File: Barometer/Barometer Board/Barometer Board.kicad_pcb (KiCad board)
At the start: 2 copper layers, 19 x 14.5 mm, 3 parts

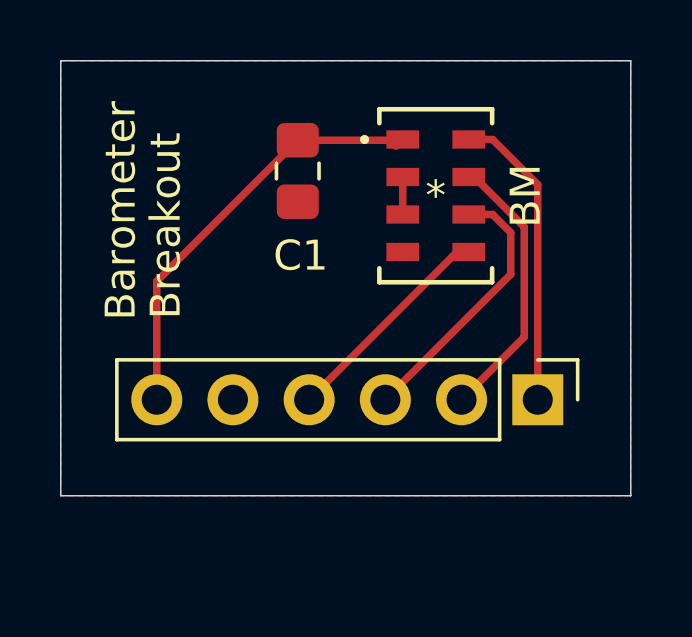
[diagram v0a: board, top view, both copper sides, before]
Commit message: Board Additions
Added the ground pour on bottom layer. Added no connect symbol on 4th pin. Added silk screen for pin outs
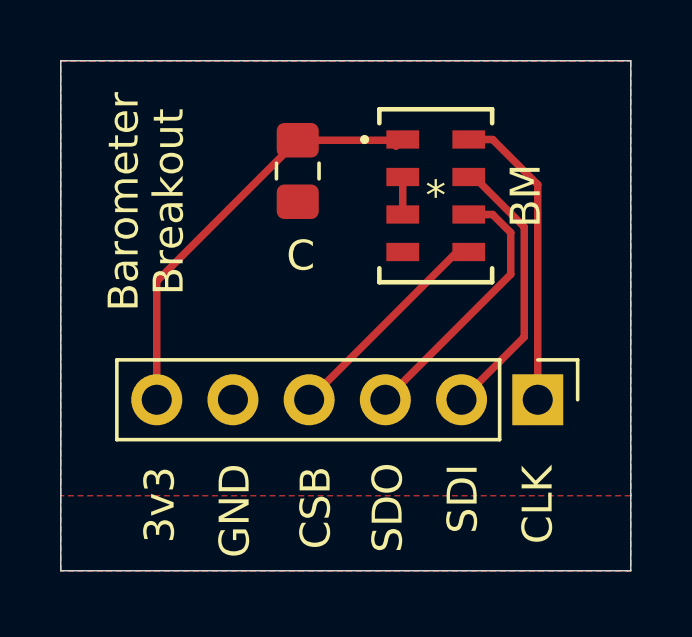
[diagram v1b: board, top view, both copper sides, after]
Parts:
- renumbered C1 to C
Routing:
- added copper zone on B.Cu, net GND
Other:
- board size 19 x 14.5 mm -> 19 x 17 mm
- board text added: "3v3"
- board text added: "CLK"
- board text added: "CSB"
- board text added: "GND"
- board text added: "SDI"
- board text added: "SDO"
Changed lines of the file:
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@@
   (general
     (thickness 1.6)
-    (drawings 6)
+    (drawings 15)
     (tracks 20)
     (zones 0)
@@
   (layers
     (0 F.Cu signal hide)
-    (31 B.Cu signal)
+    (31 B.Cu signal hide)
     (32 B.Adhes user)
     (33 F.Adhes user)
@@
     (pad_to_mask_clearance 0.05)
     (aux_axis_origin 0 0)
-    (visible_elements FFFFFF7F)
+    (visible_elements 7FFFFFFF)
     (pcbplotparams
       (layerselection 0x010fc_ffffffff)
@@
     (fp_text value MS560702BA03-50 (at 0 0) (layer F.Fab)
       (effects (font (size 1 1) (thickness 0.15)))
-    )
-    (fp_arc (start 0 -2.5019) (end 0.3048 -2.5019) (angle 180) (layer F.Fab) (width 0.1524))
-    (fp_text user * (at 0 0) (layer F.Fab)
-      (effects (font (size 1 1) (thickness 0.15)))
-    )
-    (fp_text user * (at 0 0) (layer F.SilkS)
-      (effects (font (size 1 1) (thickness 0.15)))
-    )
-    (fp_text user "Copyright 2016 Accelerated Designs. All rights reserved." (at 0 0) (layer Cmts.User)
-      (effects (font (size 0.127 0.127) (thickness 0.002)))
     )
     (fp_line (start -1.8796 2.8829) (end 1.8796 2.8829) (layer F.SilkS) (width 0.1524))
@@
     (fp_circle (center -2.3727 -1.875) (end -2.2965 -1.875) (layer F.SilkS) (width 0.1524))
     (fp_circle (center -0.254 -1.875) (end -0.1778 -1.875) (layer F.Fab) (width 0.1524))
+    (fp_arc (start 0 -2.5019) (end 0.3048 -2.5019) (angle 180) (layer F.Fab) (width 0.1524))
+    (fp_text user * (at 0 0) (layer F.Fab)
+      (effects (font (size 1 1) (thickness 0.15)))
+    )
+    (fp_text user * (at 0 0) (layer F.SilkS)
+      (effects (font (size 1 1) (thickness 0.15)))
+    )
+    (fp_text user "Copyright 2016 Accelerated Designs. All rights reserved." (at 0 0) (layer Cmts.User)
+      (effects (font (size 0.127 0.127) (thickness 0.002)))
+    )
     (pad 8 smd rect (at 1.1 -1.875) (size 1.0922 0.6096) (layers F.Cu F.Paste F.Mask)
       (net 7 /Barometer/CLK))
@@
     (tags "capacitor handsolder")
     (attr smd)
-    (fp_text reference C1 (at 2.825 -0.1 180) (layer F.SilkS)
+    (fp_text reference C (at 2.825 -0.1 180) (layer F.SilkS)
       (effects (font (size 1 1) (thickness 0.15)))
     )
@@
     )
   )
-  (gr_text Breakout (at 122 95 90) (layer F.SilkS)
-    (effects (font (size 1 1) (thickness 0.15)))
-  )
-  (gr_text Barometer (at 120.5 94.5 90) (layer F.SilkS)
+  (gr_line (start 137.5 106.5) (end 137.4 106.5) (layer Edge.Cuts) (width 0.05))
+  (gr_line (start 137.5 104) (end 137.5 106.5) (layer Edge.Cuts) (width 0.05))
+  (gr_line (start 118.5 106.5) (end 137.4 106.5) (layer Edge.Cuts) (width 0.05))
+  (gr_line (start 118.5 104) (end 118.5 106.5) (layer Edge.Cuts) (width 0.05))
+  (gr_text 3v3 (at 121.8 104.3 90) (layer F.SilkS)
+    (effects (font (size 1 1) (thickness 0.15)))
+  )
+  (gr_text GND (at 124.3 104.5 90) (layer F.SilkS)
+    (effects (font (size 1 1) (thickness 0.15)))
+  )
+  (gr_text CSB (at 127 104.4 90) (layer F.SilkS)
+    (effects (font (size 1 1) (thickness 0.15)))
+  )
+  (gr_text SDO (at 129.4 104.4 90) (layer F.SilkS)
+    (effects (font (size 1 1) (thickness 0.15)))
+  )
+  (gr_text CLK (at 134.4 104.3 90) (layer F.SilkS)
+    (effects (font (size 1 1) (thickness 0.15)))
+  )
+  (gr_text SDI (at 131.9 104.1 90) (layer F.SilkS)
+    (effects (font (size 1 1) (thickness 0.15)))
+  )
+  (gr_text Breakout (at 122.1 94.2 90) (layer F.SilkS)
+    (effects (font (size 1 1) (thickness 0.15)))
+  )
+  (gr_text Barometer (at 120.6 94.2 90) (layer F.SilkS)
     (effects (font (size 1 1) (thickness 0.15)))
   )
@@
   (gr_line (start 118.5 104) (end 118.5 89.5) (layer Edge.Cuts) (width 0.05))
   (gr_line (start 137.5 104) (end 137.5 89.5) (layer Edge.Cuts) (width 0.05))
-  (gr_line (start 118.5 104) (end 137.5 104) (layer Edge.Cuts) (width 0.05))
   (segment (start 129.675 92.35) (end 129.9 92.125) (width 0.25) (layer F.Cu) (net 1))
   (segment (start 129.875 92.15) (end 129.9 92.125) (width 0.25) (layer F.Cu) (net 1))
@@
       )
     )
+  )
+  (zone (net 2) (net_name GND) (layer F.Cu) (hatch edge 0.508)
+    (connect_pads (clearance 0.508))
+    (min_thickness 0.254)
+    (fill yes (arc_segments 32) (thermal_gap 0.508) (thermal_bridge_width 0.508))
+    (polygon
+      (pts
+        (xy 137.5 106.5) (xy 118.5 106.5) (xy 118.5 89.5) (xy 137.5 89.5)
+      )
+    )
+  )
+  (zone (net 2) (net_name GND) (layer F.Cu) (hatch edge 0.508)
+    (connect_pads (clearance 0.508))
+    (min_thickness 0.254)
+    (fill yes (arc_segments 32) (thermal_gap 0.508) (thermal_bridge_width 0.508))
+    (polygon
+      (pts
+        (xy 137.5 106.5) (xy 118.5 106.5) (xy 118.5 89.5) (xy 137.5 89.5)
+      )
+    )
+  )
+  (zone (net 2) (net_name GND) (layer B.Cu) (hatch edge 0.508)
+    (connect_pads (clearance 0.508))
+    (min_thickness 0.254)
+    (fill yes (arc_segments 32) (thermal_gap 0.508) (thermal_bridge_width 0.508))
+    (polygon
+      (pts
+        (xy 137.5 106.5) (xy 118.5 106.5) (xy 118.5 89.5) (xy 137.5 89.5)
+      )
+    )

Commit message: Fixed Minor Issues
BOOM!
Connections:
- net /Barometer/CLK renamed /Barometer/SCLK
- BM pad 4: Net-(Barometer201-Pad4) -> /Barometer/CSB
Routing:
- net /Barometer/CSB: track 7.36 -> 8.81 mm
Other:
- board text added: "SCLK"
- board text removed: "CLK"
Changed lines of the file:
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@@
     (thickness 1.6)
     (drawings 15)
-    (tracks 20)
+    (tracks 22)
     (zones 0)
     (modules 3)
-    (nets 8)
+    (nets 7)
   )
   (page A4)
@@
   (net 1 +3V3)
   (net 2 GND)
-  (net 3 "Net-(Barometer201-Pad4)")
-  (net 4 /Barometer/CSB)
-  (net 5 /Barometer/SDO)
-  (net 6 /Barometer/SDI)
-  (net 7 /Barometer/CLK)
+  (net 3 /Barometer/CSB)
+  (net 4 /Barometer/SDO)
+  (net 5 /Barometer/SDI)
+  (net 6 /Barometer/SCLK)
   (net_class Default "This is the default net class."
     (clearance 0.2)
@@
     (uvia_drill 0.1)
     (add_net +3V3)
-    (add_net /Barometer/CLK)
     (add_net /Barometer/CSB)
+    (add_net /Barometer/SCLK)
     (add_net /Barometer/SDI)
     (add_net /Barometer/SDO)
     (add_net GND)
-    (add_net "Net-(Barometer201-Pad4)")
   )
   (module "Footprint Libraries:MS560702BA03-50" (layer F.Cu)
@@
     )
     (pad 8 smd rect (at 1.1 -1.875) (size 1.0922 0.6096) (layers F.Cu F.Paste F.Mask)
-      (net 7 /Barometer/CLK))
+      (net 6 /Barometer/SCLK))
     (pad 7 smd rect (at 1.1 -0.625) (size 1.0922 0.6096) (layers F.Cu F.Paste F.Mask)
-      (net 6 /Barometer/SDI))
+      (net 5 /Barometer/SDI))
     (pad 6 smd rect (at 1.1 0.625) (size 1.0922 0.6096) (layers F.Cu F.Paste F.Mask)
-      (net 5 /Barometer/SDO))
+      (net 4 /Barometer/SDO))
     (pad 5 smd rect (at 1.1 1.875) (size 1.0922 0.6096) (layers F.Cu F.Paste F.Mask)
-      (net 4 /Barometer/CSB))
+      (net 3 /Barometer/CSB))
     (pad 4 smd rect (at -1.1 1.875) (size 1.0922 0.6096) (layers F.Cu F.Paste F.Mask)
-      (net 3 "Net-(Barometer201-Pad4)"))
+      (net 3 /Barometer/CSB))
     (pad 3 smd rect (at -1.1 0.625) (size 1.0922 0.6096) (layers F.Cu F.Paste F.Mask)
       (net 2 GND))
@@
     )
     (pad 1 thru_hole rect (at 0 0 270) (size 1.7 1.7) (drill 1) (layers *.Cu *.Mask)
-      (net 7 /Barometer/CLK))
+      (net 6 /Barometer/SCLK))
     (pad 2 thru_hole oval (at 0 2.54 270) (size 1.7 1.7) (drill 1) (layers *.Cu *.Mask)
-      (net 6 /Barometer/SDI))
+      (net 5 /Barometer/SDI))
     (pad 3 thru_hole oval (at 0 5.08 270) (size 1.7 1.7) (drill 1) (layers *.Cu *.Mask)
-      (net 5 /Barometer/SDO))
+      (net 4 /Barometer/SDO))
     (pad 4 thru_hole oval (at 0 7.62 270) (size 1.7 1.7) (drill 1) (layers *.Cu *.Mask)
-      (net 4 /Barometer/CSB))
+      (net 3 /Barometer/CSB))
     (pad 5 thru_hole oval (at 0 10.16 270) (size 1.7 1.7) (drill 1) (layers *.Cu *.Mask)
       (net 2 GND))
@@
   (gr_line (start 118.5 106.5) (end 137.4 106.5) (layer Edge.Cuts) (width 0.05))
   (gr_line (start 118.5 104) (end 118.5 106.5) (layer Edge.Cuts) (width 0.05))
-  (gr_text 3v3 (at 121.8 104.3 90) (layer F.SilkS)
-    (effects (font (size 1 1) (thickness 0.15)))
-  )
-  (gr_text GND (at 124.3 104.5 90) (layer F.SilkS)
-    (effects (font (size 1 1) (thickness 0.15)))
-  )
-  (gr_text CSB (at 127 104.4 90) (layer F.SilkS)
-    (effects (font (size 1 1) (thickness 0.15)))
-  )
-  (gr_text SDO (at 129.4 104.4 90) (layer F.SilkS)
-    (effects (font (size 1 1) (thickness 0.15)))
-  )
-  (gr_text CLK (at 134.4 104.3 90) (layer F.SilkS)
-    (effects (font (size 1 1) (thickness 0.15)))
-  )
-  (gr_text SDI (at 131.9 104.1 90) (layer F.SilkS)
+  (gr_text 3v3 (at 121.8 104.1 90) (layer F.SilkS)
+    (effects (font (size 1 1) (thickness 0.15)))
+  )
+  (gr_text GND (at 124.3 104.3 90) (layer F.SilkS)
+    (effects (font (size 1 1) (thickness 0.15)))
+  )
+  (gr_text CSB (at 127 104.2 90) (layer F.SilkS)
+    (effects (font (size 1 1) (thickness 0.15)))
+  )
+  (gr_text SDO (at 129.4 104.2 90) (layer F.SilkS)
+    (effects (font (size 1 1) (thickness 0.15)))
+  )
+  (gr_text SCLK (at 134.4 104.5 90) (layer F.SilkS)
+    (effects (font (size 1 1) (thickness 0.15)))
+  )
+  (gr_text SDI (at 131.9 103.9 90) (layer F.SilkS)
     (effects (font (size 1 1) (thickness 0.15)))
   )
@@
   (segment (start 129.9 93.375) (end 129.9 94.625) (width 0.25) (layer F.Cu) (net 2))
   (segment (start 126.625 94.625) (end 126.4 94.4) (width 0.25) (layer F.Cu) (net 2))
-  (segment (start 131.705 95.875) (end 132.1 95.875) (width 0.25) (layer F.Cu) (net 4))
-  (segment (start 126.78 100.8) (end 131.705 95.875) (width 0.25) (layer F.Cu) (net 4))
-  (segment (start 129.32 100.8) (end 133.49998 96.62002) (width 0.25) (layer F.Cu) (net 5))
-  (segment (start 133.49998 95.22888) (end 132.8961 94.625) (width 0.25) (layer F.Cu) (net 5))
-  (segment (start 132.8961 94.625) (end 132.1 94.625) (width 0.25) (layer F.Cu) (net 5))
-  (segment (start 133.49998 96.62002) (end 133.49998 95.22888) (width 0.25) (layer F.Cu) (net 5))
-  (segment (start 132.285902 93.375) (end 132.1 93.375) (width 0.25) (layer F.Cu) (net 6))
-  (segment (start 133.949989 95.039087) (end 132.285902 93.375) (width 0.25) (layer F.Cu) (net 6))
-  (segment (start 133.949989 98.710011) (end 133.949989 95.039087) (width 0.25) (layer F.Cu) (net 6))
-  (segment (start 131.86 100.8) (end 133.949989 98.710011) (width 0.25) (layer F.Cu) (net 6))
-  (segment (start 132.8961 92.125) (end 132.1 92.125) (width 0.25) (layer F.Cu) (net 7))
-  (segment (start 134.4 93.6289) (end 132.8961 92.125) (width 0.25) (layer F.Cu) (net 7))
-  (segment (start 134.4 100.8) (end 134.4 93.6289) (width 0.25) (layer F.Cu) (net 7))
-  (zone (net 2) (net_name GND) (layer F.Cu) (hatch edge 0.508)
-    (connect_pads (clearance 0.508))
-    (min_thickness 0.254)
-    (fill yes (arc_segments 32) (thermal_gap 0.508) (thermal_bridge_width 0.508))
-    (polygon
-      (pts
-        (xy 137.5 104) (xy 118.5 104) (xy 118.5 89.5) (xy 137.5 89.5)
-      )
-    )
-  )
-  (zone (net 2) (net_name GND) (layer F.Cu) (hatch edge 0.508)
+  (segment (start 131.705 95.875) (end 132.1 95.875) (width 0.25) (layer F.Cu) (net 3))
+  (segment (start 129.9 95.875) (end 132.1 95.875) (width 0.25) (layer F.Cu) (net 3))
+  (segment (start 126.78 98.995) (end 129.9 95.875) (width 0.25) (layer F.Cu) (net 3))
+  (segment (start 126.78 100.8) (end 126.78 98.995) (width 0.25) (layer F.Cu) (net 3))
+  (segment (start 129.32 100.8) (end 133.49998 96.62002) (width 0.25) (layer F.Cu) (net 4))
+  (segment (start 133.49998 95.22888) (end 132.8961 94.625) (width 0.25) (layer F.Cu) (net 4))
+  (segment (start 132.8961 94.625) (end 132.1 94.625) (width 0.25) (layer F.Cu) (net 4))
+  (segment (start 133.49998 96.62002) (end 133.49998 95.22888) (width 0.25) (layer F.Cu) (net 4))
+  (segment (start 132.285902 93.375) (end 132.1 93.375) (width 0.25) (layer F.Cu) (net 5))
+  (segment (start 133.949989 95.039087) (end 132.285902 93.375) (width 0.25) (layer F.Cu) (net 5))
+  (segment (start 133.949989 98.710011) (end 133.949989 95.039087) (width 0.25) (layer F.Cu) (net 5))
+  (segment (start 131.86 100.8) (end 133.949989 98.710011) (width 0.25) (layer F.Cu) (net 5))
+  (segment (start 132.8961 92.125) (end 132.1 92.125) (width 0.25) (layer F.Cu) (net 6))
+  (segment (start 134.4 93.6289) (end 132.8961 92.125) (width 0.25) (layer F.Cu) (net 6))
+  (segment (start 134.4 100.8) (end 134.4 93.6289) (width 0.25) (layer F.Cu) (net 6))
+  (zone (net 2) (net_name GND) (layer B.Cu) (hatch edge 0.508)
     (connect_pads (clearance 0.508))
     (min_thickness 0.254)
@@
     (connect_pads (clearance 0.508))
     (min_thickness 0.254)
-    (fill yes (arc_segments 32) (thermal_gap 0.508) (thermal_bridge_width 0.508))
-    (polygon
-      (pts
-        (xy 137.5 106.5) (xy 118.5 106.5) (xy 118.5 89.5) (xy 137.5 89.5)
-      )
-    )
-  )
-  (zone (net 2) (net_name GND) (layer B.Cu) (hatch edge 0.508)
-    (connect_pads (clearance 0.508))
-    (min_thickness 0.254)
